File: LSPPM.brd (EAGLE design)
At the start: 95.5 x 90.3 mm, 341 parts, among them IC1 ATMEGA328P QFN32, IC10 ATMEGA328P QFN32, IC11 ATMEGA328P QFN32, IC12 ATMEGA328P QFN32, IC13 ATMEGA328P QFN32, IC14 ATMEGA328P QFN32, IC15 ATMEGA328P QFN32, IC16 ATMEGA328P QFN32, IC17 TXB0104, IC18 TMP102, IC19 TMP102, IC2 ATMEGA328P QFN32, IC20 ATMEGA2561-16MU, IC21 MAX4372F, IC22 MAX4372F, IC23 MUX-74HC4067-QFNSMT, IC24 MUX-74HC4067-QFNSMT, IC25 TCA9555QFN, IC3 ATMEGA328P QFN32, IC4 ATMEGA328P QFN32, IC5 ATMEGA328P QFN32, IC6 ATMEGA328P QFN32, IC7 ATMEGA328P QFN32, IC8 ATMEGA328P QFN32, IC9 ATMEGA328P QFN32, P1 microSD, Q1 RJU003N03 N-MOSFET, Q10 RJU003N03 N-MOSFET, Q11 RJU003N03 N-MOSFET, Q12 RJU003N03 N-MOSFET, Q13 RJU003N03 N-MOSFET, Q14 RJU003N03 N-MOSFET, Q15 RJU003N03 N-MOSFET, Q16 RJU003N03 N-MOSFET, Q17 RJU003N03 N-MOSFET, Q18 RJU003N03 N-MOSFET, Q19 RJU003N03 N-MOSFET, Q2 RJU003N03 N-MOSFET, Q20 RJU003N03 N-MOSFET, Q21 RJU003N03 N-MOSFET, Q22 RJU003N03 N-MOSFET, Q23 RJU003N03 N-MOSFET, Q24 RJU003N03 N-MOSFET, Q25 RJU003N03 N-MOSFET, Q26 RJU003N03 N-MOSFET, Q27 RJU003N03 N-MOSFET, Q28 RJU003N03 N-MOSFET, Q29 RJU003N03 N-MOSFET, Q3 RJU003N03 N-MOSFET, Q30 RJU003N03 N-MOSFET, Q31 RJU003N03 N-MOSFET, Q32 RJU003N03 N-MOSFET, Q33 RJU003N03 N-MOSFET, Q34 RJU003N03 N-MOSFET, Q35 RJU003N03 N-MOSFET, Q36 RJU003N03 N-MOSFET, Q37 RJU003N03 N-MOSFET, Q38 RJU003N03 N-MOSFET, Q39 RJU003N03 N-MOSFET, Q4 RJU003N03 N-MOSFET, Q40 RJU003N03 N-MOSFET, Q41 RJU003N03 N-MOSFET, Q42 RJU003N03 N-MOSFET, Q43 RJU003N03 N-MOSFET, Q44 RJU003N03 N-MOSFET, Q45 RJU003N03 N-MOSFET, Q46 RJU003N03 N-MOSFET, Q5 RJU003N03 N-MOSFET, Q6 RJU003N03 N-MOSFET, Q7 RJU003N03 N-MOSFET, Q8 RJU003N03 N-MOSFET, Q9 RJU003N03 N-MOSFET, SW1 ADG801 SOT23-6, SW10 ADG801 SOT23-6, SW11 ADG801 SOT23-6, SW12 ADG801 SOT23-6, SW13 ADG801 SOT23-6, SW14 ADG801 SOT23-6, SW15 ADG801 SOT23-6, SW16 ADG801 SOT23-6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

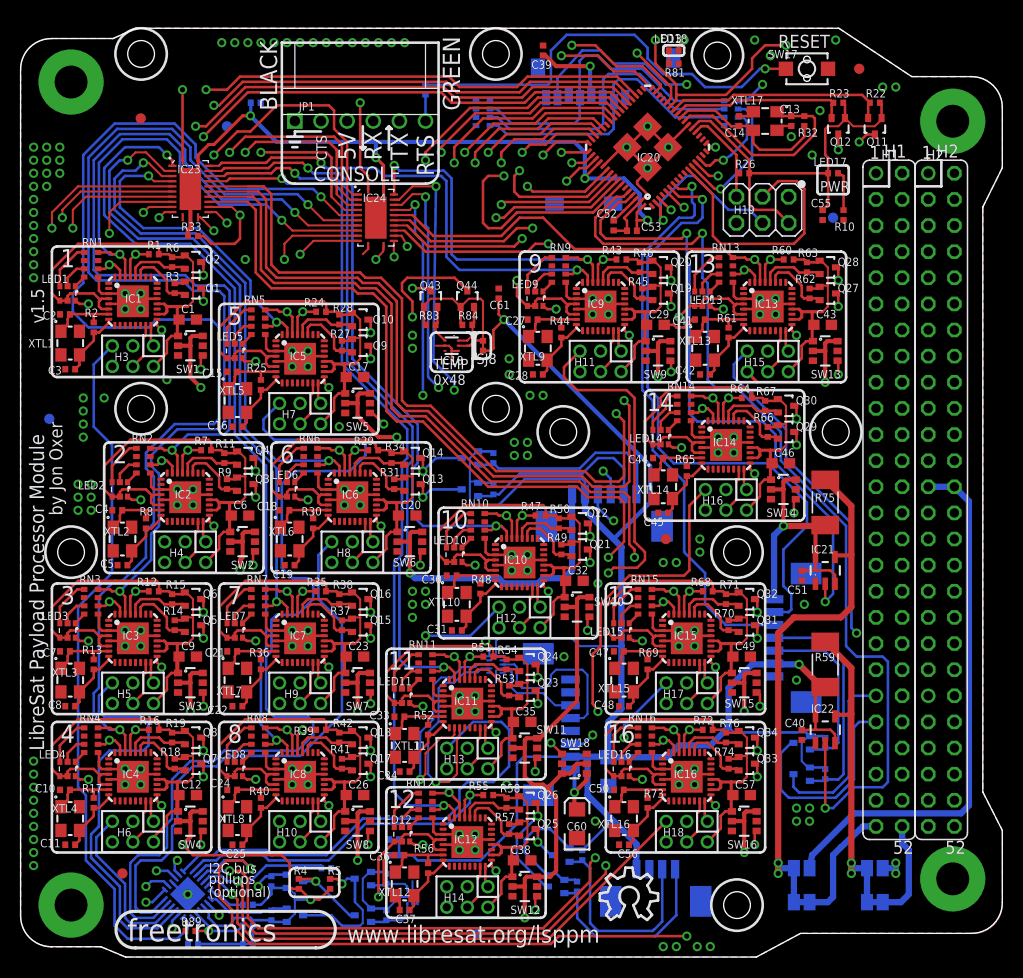
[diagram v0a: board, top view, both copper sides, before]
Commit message: Replaced most parts using SuperHouse library to add 3D models
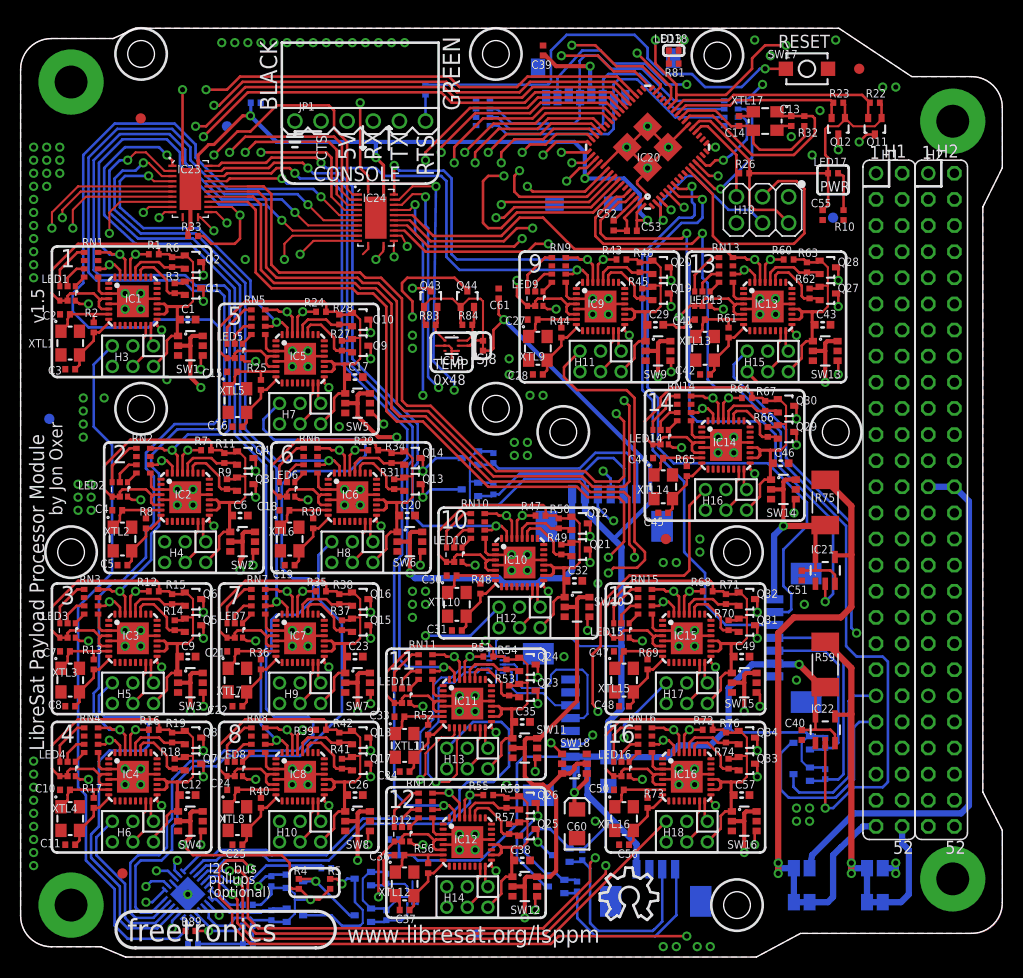
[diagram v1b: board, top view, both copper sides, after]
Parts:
- C1, C12, C17, C20, C23, C26, C29, C32, C35, C38, C43, C46, C49, C57, C6, C9: device freetronics-jon:C0603 -> SuperHouse-DiscreteSemi:C0603
- C10, C11, C13, C14, C15, C16, C18, C19, C2, C21, C22, C24, C25, C27, C28, C3, C30, C31, C33, C34, C36, C37, C39, C4, C40, C41, C42, C44, C45, C47, C48, C5, C50, C51, C52, C53, C54, C55, C56, C58, C61, C62, C7, C8: device freetronics-jon:0402C -> SuperHouse-DiscreteSemi:C0402
- C59, C60: device freetronics-jon:EIA3216 -> SuperHouse-DiscreteSemi:EIA3216
- H1, H2: value CUBESATBUSH -> CUBESATBUS-ST; device freetronics-jon:CUBESATBUS -> SuperHouse-Connectors:CUBESATBUS-ST
- H19: device freetronics-jon:2X03PTH -> SuperHouse-Connectors:2X03-ICSP
- IC1, IC10, IC11, IC12, IC13, IC14, IC15, IC16, IC2, IC3, IC4, IC5, IC6, IC7, IC8, IC9: device freetronics-jon:MLF32 -> SuperHouse-MCUs:MLF32
- IC18, IC19: device freetronics-jon:SOT563 -> SuperHouse-Sensors:SOT563
- JP1: device freetronics-master-v1:MOLEX-1X6-RA -> SuperHouse-Connectors:1X06-P-RA
- LED17, LED18: device freetronics-jon:LED-0402 -> SuperHouse-LEDs:LED-0402
- P1: device freetronics-master-v1.1:MICRO-SD-SOCKET-PP -> SuperHouse-Connectors:MICRO-SD-SOCKET-PP
- Q1, Q10, Q11, Q12, Q13, Q14, Q15, Q16, Q17, Q18, Q19, Q2, Q20, Q21, Q22, Q23, Q24, Q25, Q26, Q27, Q28, Q29, Q3, Q30, Q31, Q32, Q33, Q34, Q35, Q36, Q37, Q38, Q39, Q4, Q40, Q41, Q42, Q43, Q44, Q45, Q46, Q5, Q6, Q7, Q8, Q9: device freetronics-jon:SOT32-3 -> SuperHouse-DiscreteSemi:SOT32-3
- R1, R10, R11, R12, R13, R14, R15, R16, R17, R18, R19, R2, R20, R21, R22, R23, R24, R25, R26, R27, R28, R29, R3, R30, R31, R32, R33, R34, R35, R36, R37, R38, R39, R4, R40, R41, R42, R43, R44, R45, R46, R47, R48, R49, R5, R50, R51, R52, R53, R54, R55, R56, R57, R58, R6, R60, R61, R62, R63, R64, R65, R66, R67, R68, R69, R7, R70, R71, R72, R73, R74, R76, R77, R78, R79, R8, R80, R81, R82, R83, R84, R85, R86, R87, R88, R89, R9, R90: device freetronics-jon:0402 -> SuperHouse-DiscreteSemi:R0402
- R59, R75: device freetronics-original:R2010 -> SuperHouse-DiscreteSemi:R2010
- RN1, RN10, RN11, RN12, RN13, RN14, RN15, RN16, RN2, RN3, RN4, RN5, RN6, RN7, RN8, RN9: device resistor-dil:CAY16 -> SuperHouse-DiscreteSemi:CAY16
- RN17, RN18: device freetronics-master-v1:CAY16 -> SuperHouse-DiscreteSemi:CAY16
- SW17: device freetronics-master-v1:TACTILE_SWITCH_SMD_2PIN_TINY -> SuperHouse-Switches:TACTILE_SMT_3X4X2
- X1: device con-molex:53398-06 -> SuperHouse-Connectors:53398-06
- X2: device con-molex:53398-08 -> SuperHouse-Connectors:53398-08
- X3: device con-molex:53398-07 -> SuperHouse-Connectors:53398-07
- XTL1, XTL10, XTL11, XTL12, XTL13, XTL14, XTL15, XTL16, XTL17, XTL2, XTL3, XTL4, XTL5, XTL6, XTL7, XTL8, XTL9: device freetronics-jon:CRYSTAL-SMD-3X2 -> SuperHouse-Oscillators:CRYSTAL-SMD-3X2
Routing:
- net GND: track 280.2 -> 274.9 mm
